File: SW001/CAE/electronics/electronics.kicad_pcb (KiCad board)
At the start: 2 copper layers, 88 x 84 mm, 4 parts, among them J1 Conn_02x30_Counter_Clockwise

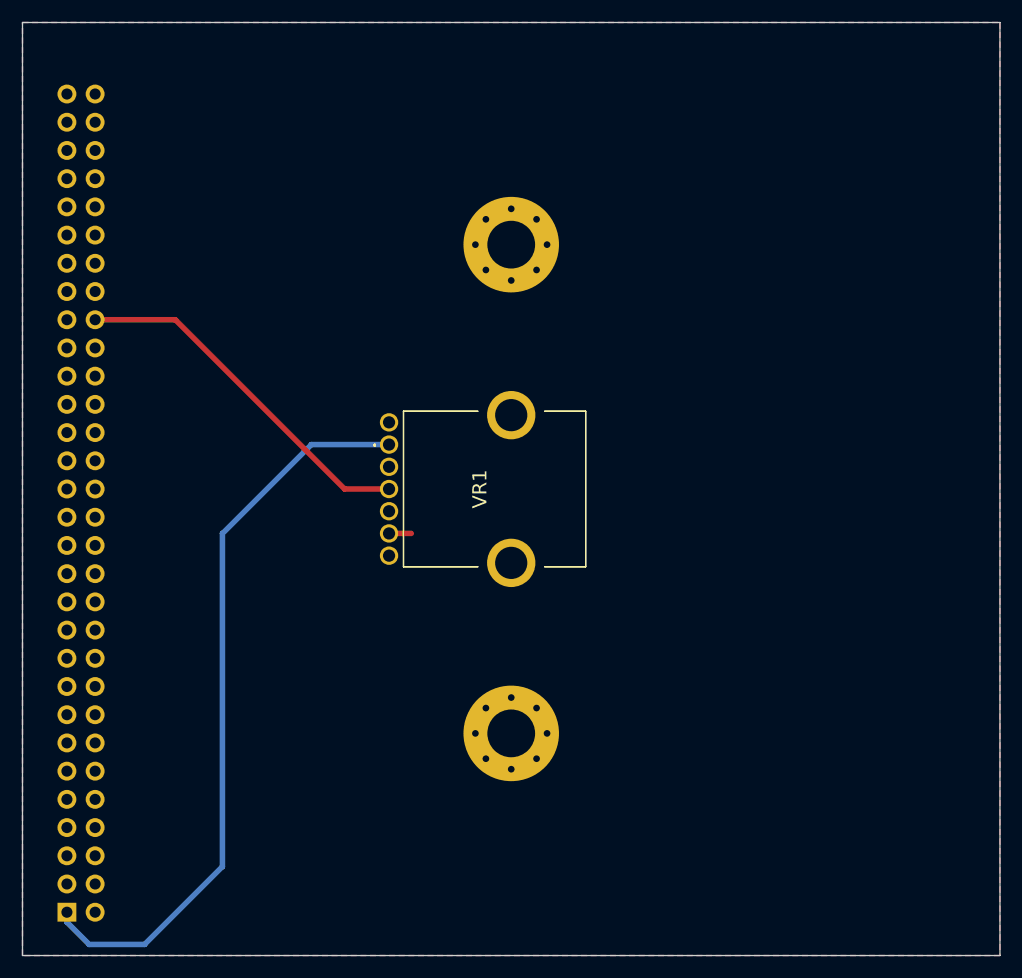
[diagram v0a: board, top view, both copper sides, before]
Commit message: Planet gear updated Signed-off-by: Reisen-Wandern-Tauchen <webmaster@reisen-wandern-tauchen.at>
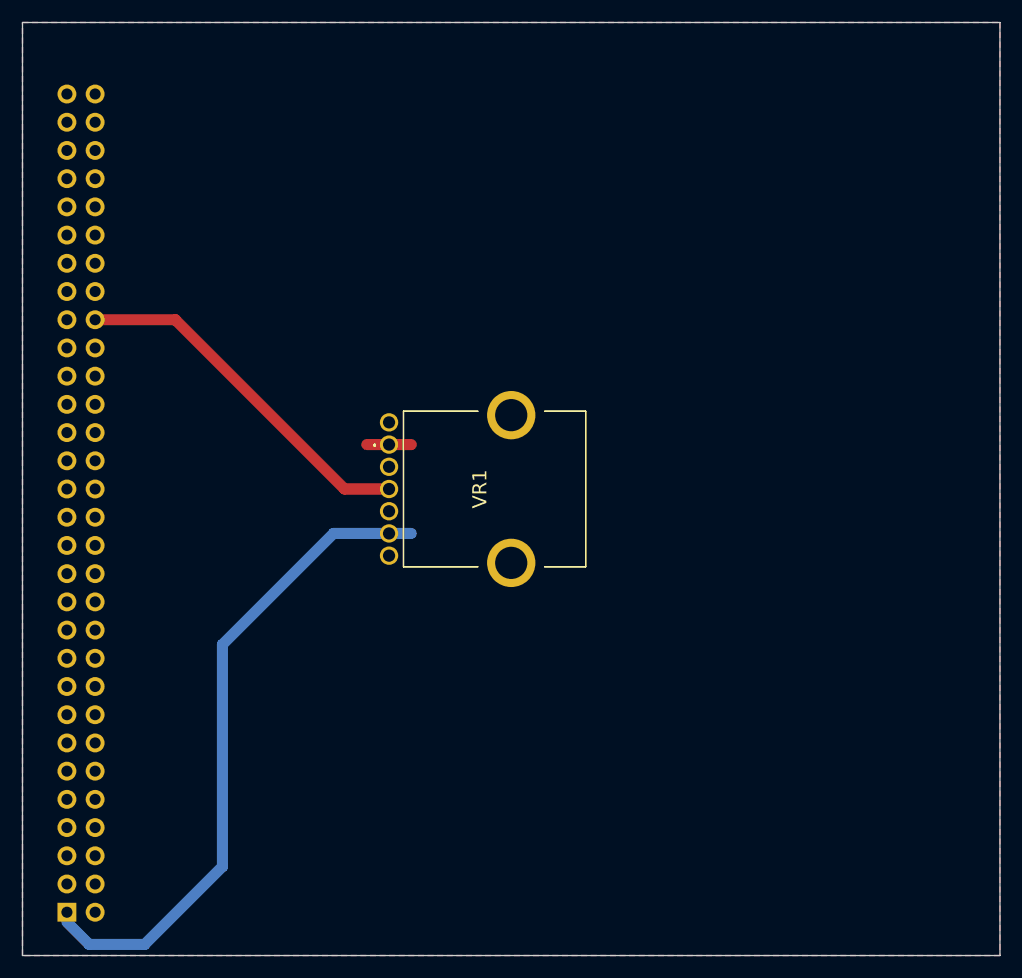
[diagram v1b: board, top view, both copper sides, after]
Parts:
- removed REF** (x2): MountingHole_4.3mm_M4_Pad_Via, MountingHole:MountingHole_4.3mm_M4_Pad_Via
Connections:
- VR1 pad 1: 3V3 -> GND
- VR1 pad 5: GND -> 3V3
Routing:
- net 3V3: track 66.9 -> 59.8 mm
- net GND: track 2.00 -> 4.00 mm
- added copper zone on B.Cu, net 3V3
- removed copper zone on B.Cu, net GND
